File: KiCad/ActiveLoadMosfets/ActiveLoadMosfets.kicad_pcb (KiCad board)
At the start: 2 copper layers, 83.2 x 161.9 mm, 74 parts, among them J1 Conn_01x02_Male, J2 Conn_02x03_Odd_Even, Q1 STP60NF06L, Q2 STP60NF06L, Q3 STP60NF06L, Q4 STP60NF06L, Q5 STP60NF06L, Q6 STP60NF06L, Q7 IRLML2244, Q8 IRLML2244, Q9 IRLML2244, SW1 SW_SPST, SW2 SW_SPDT, U1 LM7322, U2 LM78M12, U3 ATxmega32E5-AU, U4 LED-3digits, U5 LM78M33, U6 SCT2167, U7 SCT2167, U8 LED-3digits

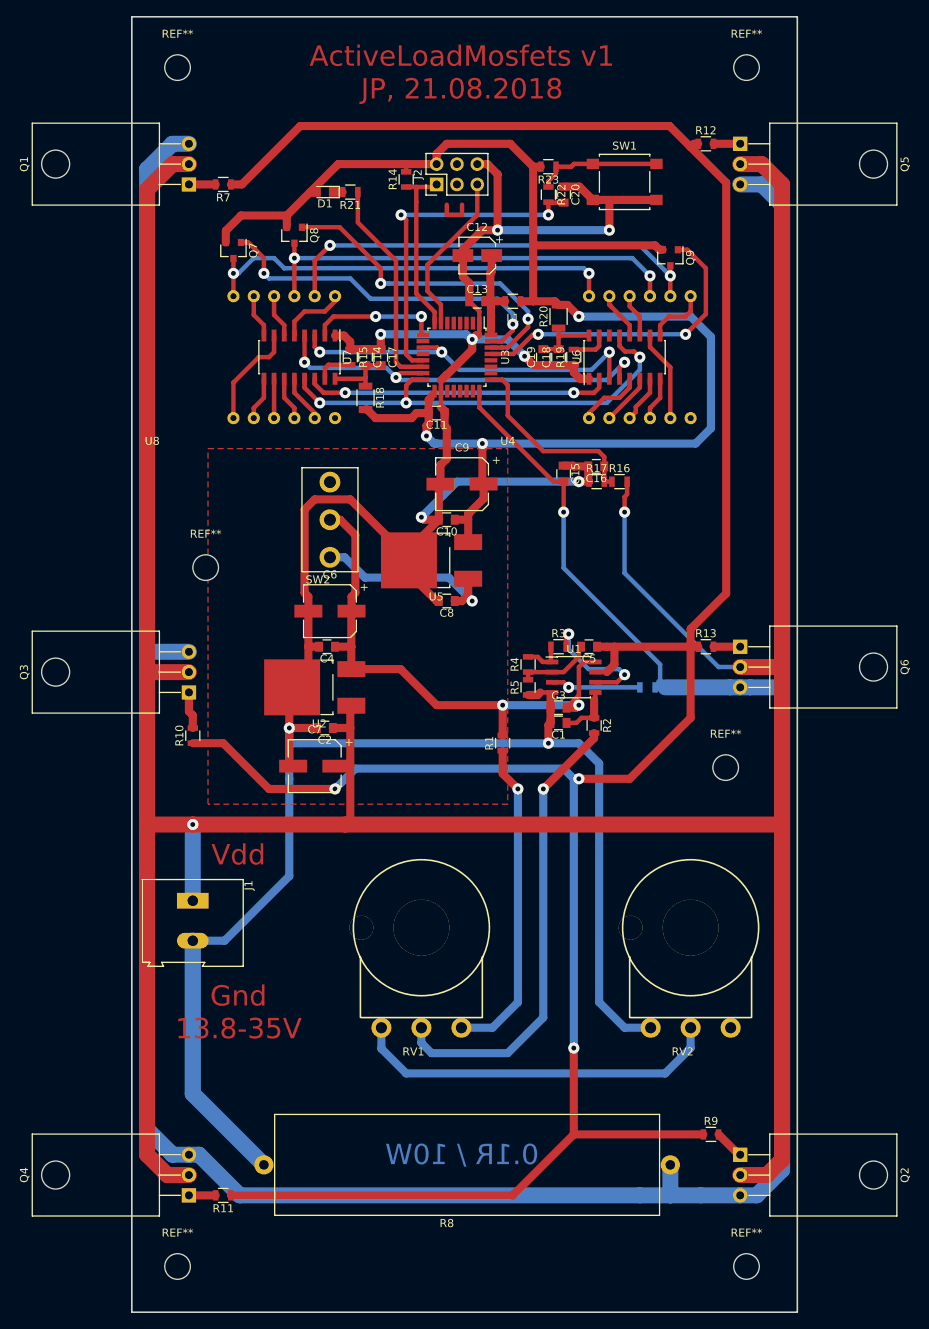
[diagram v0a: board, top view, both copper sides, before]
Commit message: New Atmel Studio project for ActiveLoadMosfets
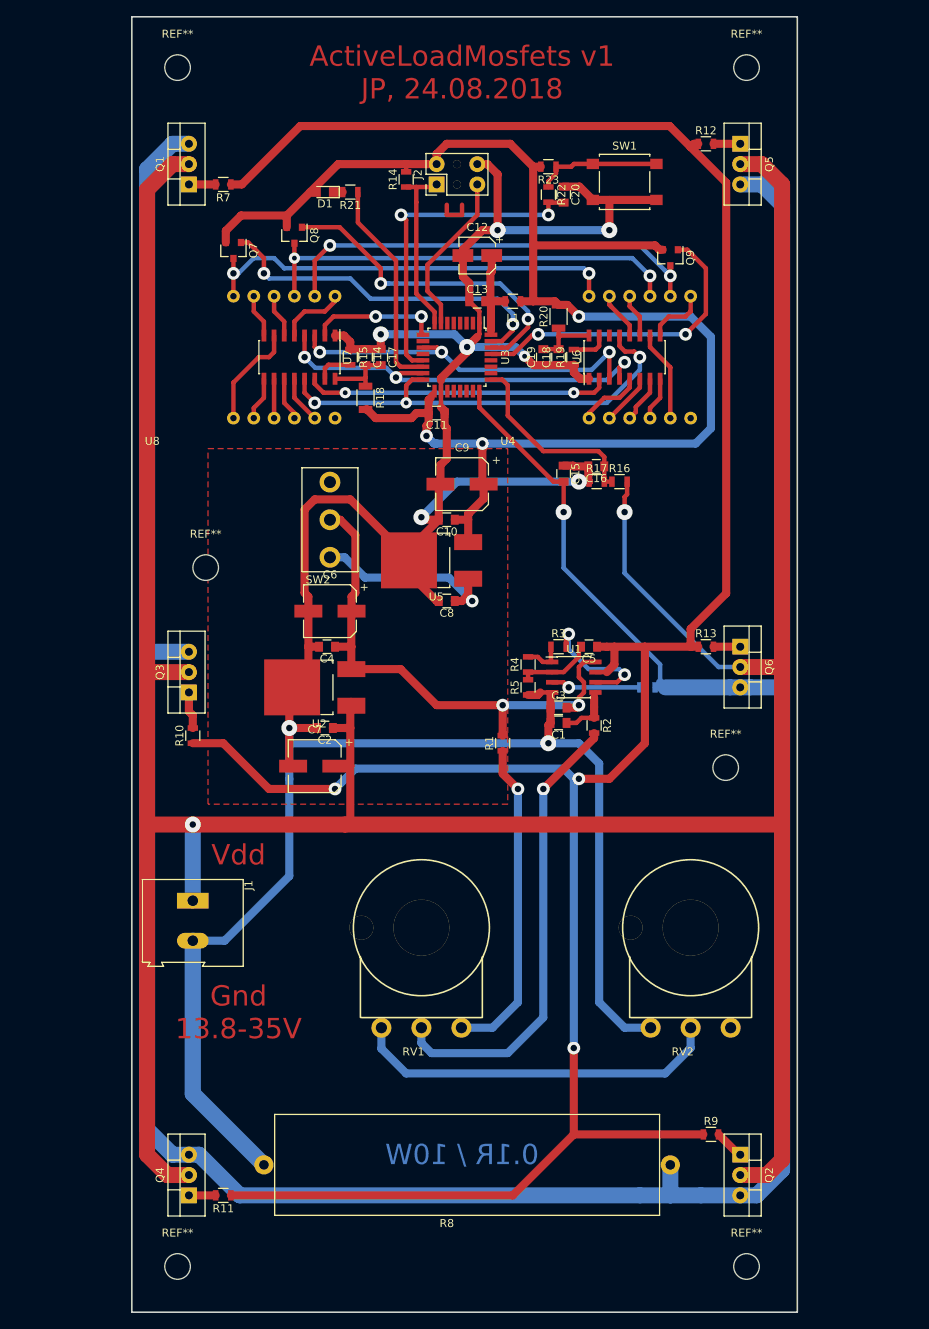
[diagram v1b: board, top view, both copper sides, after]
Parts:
- Q1, Q2, Q3, Q4, Q5, Q6: footprint TO_SOT_Packages_THT:TO-220-3_Horizontal -> TO_SOT_Packages_THT:TO-220-3_Vertical
- U1: value LM7322 -> TLV2372
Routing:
- net Net-(C5-Pad1): track 331.7 -> 327.6 mm
- net GND: track 372.1 -> 371.6 mm
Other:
- net class Default: via_dia 1.4 -> 1.6; via_drill 0.6 -> 0.8
- net class SmallPower: via_dia 1.4 -> 1.6; via_drill 0.6 -> 0.8
- board text added: "ActiveLoadMosfets v1 JP, 24.08.2018"
- board text removed: "ActiveLoadMosfets v1 JP, 21.08.2018"

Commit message: More c++ code, bug fixes on the PCB
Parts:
- added C21: 10u, Capacitors_SMD:CP_Elec_4x5.8, F.Cu at (116.2, 73.0)
- added R24: 1k1, Resistors_SMD:R_0805, F.Cu at (117.5, 68.6)
- C5: value 3n3 -> 1n
- R15, R19: value 1k -> 5k
- R16: value 1k -> 47k
- R17: value 1k -> 1k1
- R4: value 5k -> 5k / 47k ?
- moved L1 6.38 mm to (113.0, 42.5)
- moved C15 2.56 mm to (120.0, 72.7), turned to 90 degrees
- moved R16 2.54 mm to (128.3, 71.4)
- moved R17 2.54 mm to (125.4, 71.4)
- moved C16 2.54 mm to (125.4, 69.5)
- turned SW2 to 180 degrees
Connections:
- C15 pad 2: CURRENT -> Net-(C15-Pad2)
- J2 pad 1: PDI_CLK -> PDI_DATA
- J2 pad 5: PDI_DATA -> PDI_CLK
- Q1 pad 3: CURRENT -> Net-(C15-Pad2)
- Q2 pad 3: CURRENT -> Net-(C15-Pad2)
- Q3 pad 3: CURRENT -> Net-(C15-Pad2)
- Q4 pad 3: CURRENT -> Net-(C15-Pad2)
- Q5 pad 3: CURRENT -> Net-(C15-Pad2)
- Q6 pad 3: CURRENT -> Net-(C15-Pad2)
- R3 pad 2: Net-(R3-Pad2) -> Net-(C5-Pad2)
- R4 pad 1: Net-(C5-Pad2) -> Net-(R4-Pad1)
- R5 pad 2: Net-(C5-Pad2) -> Net-(R4-Pad1)
- R6 pad 1: CURRENT -> Net-(C15-Pad2)
- R8 pad 1: CURRENT -> Net-(C15-Pad2)
- U1 pad 2: Net-(C5-Pad2) -> Net-(R4-Pad1)
- U1 pad 6: Net-(R3-Pad2) -> Net-(C5-Pad2)
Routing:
- net Net-(C15-Pad2): track 0.00 -> 400.1 mm, vias 0 -> 1
- net CURRENT: track 409.9 -> 15.6 mm, vias 1 -> 0
- net Net-(R3-Pad2): track 16.6 -> 0.00 mm, vias 2 -> 0
- net Net-(C5-Pad2): track 9.48 -> 18.5 mm, vias 0 -> 2
- net Net-(C8-Pad1): track 24.9 -> 33.0 mm
- net PDI_CLK: track 21.9 -> 28.9 mm, vias 0 -> 1
- net Net-(R4-Pad1): track 0.00 -> 3.98 mm
- net +3V3: track 187.5 -> 183.8 mm
- net GND: track 371.6 -> 374.6 mm, vias 9 -> 7
- net PDI_DATA: track 20.6 -> 18.0 mm
- net SWITCH: track 42.0 -> 40.9 mm
- net /+3.3Va: track 12.8 -> 13.9 mm
- net VDD: track 416.8 -> 415.7 mm
- net VOLTAGE: track 24.4 -> 25.3 mm
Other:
- board text added: "ActiveLoadMosfets v2-snap JP, 17.09.2018"
- board text removed: "ActiveLoadMosfets v1 JP, 24.08.2018"

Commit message: BCB fixes and cpp code mostly done
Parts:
- Q1: value STP60NF06L -> STP60NF06L / STP9NK60Z
- R15, R19: value 5k -> 15k
- R4: value 5k / 47k ? -> 6k8
- U2: value LM78M12 -> LM78M09
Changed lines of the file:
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@@
       (effects (font (size 1 1) (thickness 0.15)))
     )
-    (fp_text value "5k / 47k ?" (at 0 1.75 90) (layer F.Fab)
+    (fp_text value 6k8 (at 0 1.75 90) (layer F.Fab)
       (effects (font (size 1 1) (thickness 0.15)))
     )
@@
       (effects (font (size 1 1) (thickness 0.15)))
     )
-    (fp_text value LM78M12 (at -0.625 4.8 180) (layer F.Fab)
+    (fp_text value LM78M09 (at -0.625 4.8 180) (layer F.Fab)
       (effects (font (size 1 1) (thickness 0.15)))
     )
@@
       (effects (font (size 1 1) (thickness 0.15)))
     )
-    (fp_text value 5k (at 0 1.75 270) (layer F.Fab)
+    (fp_text value 15k (at 0 1.75 270) (layer F.Fab)
       (effects (font (size 1 1) (thickness 0.15)))
     )
@@
       (effects (font (size 1 1) (thickness 0.15)))
     )
-    (fp_text value 5k (at 0 1.75 90) (layer F.Fab)
+    (fp_text value 15k (at 0 1.75 90) (layer F.Fab)
       (effects (font (size 1 1) (thickness 0.15)))
     )
@@
       (effects (font (size 1 1) (thickness 0.15)))
     )
-    (fp_text value STP60NF06L (at 2.54 3.92 90) (layer F.Fab)
+    (fp_text value "STP60NF06L / STP9NK60Z" (at 2.54 3.92 90) (layer F.Fab)
       (effects (font (size 1 1) (thickness 0.15)))
     )
@@
   (segment (start 120.65 95.885) (end 120.65 94.615) (width 0.5588) (layer F.Cu) (net 4))
   (segment (start 120.65 94.615) (end 121.285 93.98) (width 0.5588) (layer F.Cu) (net 4))
+  (via (at 126.365 95.57) (size 1.6) (drill 0.8) (layers F.Cu B.Cu) (net 5))
+  (segment (start 122.715 96.52) (end 125.415 96.52) (width 0.5588) (layer F.Cu) (net 5))
+  (segment (start 125.415 96.52) (end 126.365 95.57) (width 0.5588) (layer F.Cu) (net 5))
+  (segment (start 119.06 90.175) (end 119.06 92.075) (width 0.5588) (layer F.Cu) (net 5))
+  (via (at 119.38 90.49) (size 1.6) (drill 0.8) (layers F.Cu B.Cu) (net 5))
+  (segment (start 119.38 90.49) (end 119.38 92.395) (width 0.5588) (layer B.Cu) (net 5))
+  (segment (start 119.38 92.395) (end 121.855001 94.870001) (width 0.5588) (layer B.Cu) (net 5))
+  (segment (start 121.855001 94.870001) (end 125.665001 94.870001) (width 0.5588) (layer B.Cu) (net 5))
+  (segment (start 125.665001 94.870001) (end 126.365 95.57) (width 0.5588) (layer B.Cu) (net 5))
+  (segment (start 119.38 90.49) (end 119.06 90.175) (width 0.5588) (layer F.Cu) (net 5))
+  (segment (start 119.06 92.075) (end 120.92 92.075) (width 0.5588) (layer F.Cu) (net 5))
   (segment (start 78.516 34.29) (end 85.816 26.99) (width 1.016) (layer F.Cu) (net 6))
   (segment (start 77.15 34.29) (end 78.516 34.29) (width 1.016) (layer F.Cu) (net 6))
@@
   (segment (start 117.16 93.825) (end 117.315 93.98) (width 0.5588) (layer F.Cu) (net 15))
   (segment (start 117.16 92.075) (end 117.16 93.825) (width 0.5588) (layer F.Cu) (net 15))
-  (via (at 126.365 95.57) (size 1.6) (drill 0.8) (layers F.Cu B.Cu) (net 5))
-  (segment (start 122.715 96.52) (end 125.415 96.52) (width 0.5588) (layer F.Cu) (net 5))
-  (segment (start 125.415 96.52) (end 126.365 95.57) (width 0.5588) (layer F.Cu) (net 5))
-  (segment (start 119.06 90.175) (end 119.06 92.075) (width 0.5588) (layer F.Cu) (net 5))
-  (via (at 119.38 90.49) (size 1.6) (drill 0.8) (layers F.Cu B.Cu) (net 5))
-  (segment (start 119.38 90.49) (end 119.38 92.395) (width 0.5588) (layer B.Cu) (net 5))
-  (segment (start 119.38 92.395) (end 121.855001 94.870001) (width 0.5588) (layer B.Cu) (net 5))
-  (segment (start 121.855001 94.870001) (end 125.665001 94.870001) (width 0.5588) (layer B.Cu) (net 5))
-  (segment (start 125.665001 94.870001) (end 126.365 95.57) (width 0.5588) (layer B.Cu) (net 5))
-  (segment (start 119.38 90.49) (end 119.06 90.175) (width 0.5588) (layer F.Cu) (net 5))
-  (segment (start 119.06 92.075) (end 120.92 92.075) (width 0.5588) (layer F.Cu) (net 5))
   (via (at 119.38 97.155) (size 1.6) (drill 0.8) (layers F.Cu B.Cu) (net 16))
   (segment (start 117.315 96.52) (end 118.745 96.52) (width 0.5588) (layer F.Cu) (net 16))
@@
   (segment (start 116.205 66.675) (end 116.205 68.58) (width 0.5588) (layer F.Cu) (net 19))
   (segment (start 116.205 68.58) (end 116.205 71.225) (width 0.5588) (layer F.Cu) (net 19))
-  (segment (start 71.905 92.71) (end 66.675 92.71) (width 2) (layer B.Cu) (net 60))
-  (segment (start 146.05 157.48) (end 142.875 160.655) (width 2) (layer B.Cu) (net 60))
-  (segment (start 142.875 160.655) (end 140.82 160.655) (width 2) (layer B.Cu) (net 60))
-  (segment (start 142.092792 97.155) (end 146.05 97.155) (width 2) (layer B.Cu) (net 60))
-  (segment (start 140.82 97.155) (end 142.092792 97.155) (width 2) (layer B.Cu) (net 60))
-  (segment (start 146.05 97.155) (end 146.05 157.48) (width 2) (layer B.Cu) (net 60))
-  (segment (start 140.82 160.655) (end 135.89 160.655) (width 2) (layer B.Cu) (net 60))
-  (segment (start 66.675 32.385) (end 66.675 92.71) (width 2) (layer B.Cu) (net 60))
-  (segment (start 71.905 29.21) (end 69.85 29.21) (width 2) (layer B.Cu) (net 60))
-  (segment (start 69.85 29.21) (end 66.675 32.385) (width 2) (layer B.Cu) (net 60))
-  (segment (start 69.85 155.575) (end 71.905 155.575) (width 2) (layer B.Cu) (net 60))
-  (segment (start 66.675 92.71) (end 66.675 152.4) (width 2) (layer B.Cu) (net 60))
-  (segment (start 66.675 152.4) (end 69.85 155.575) (width 2) (layer B.Cu) (net 60))
-  (segment (start 140.82 34.29) (end 143.51 34.29) (width 2) (layer B.Cu) (net 60))
-  (segment (start 143.51 34.29) (end 146.05 36.83) (width 2) (layer B.Cu) (net 60))
-  (segment (start 146.05 36.83) (end 146.05 97.155) (width 2) (layer B.Cu) (net 60))
-  (segment (start 140.82 97.155) (end 139.547208 97.155) (width 2) (layer B.Cu) (net 60))
-  (segment (start 139.547208 97.155) (end 131.445 97.155) (width 2) (layer B.Cu) (net 60))
-  (segment (start 131.445 97.155) (end 130.81 96.52) (width 1.016) (layer B.Cu) (net 60))
-  (segment (start 130.175 97.155) (end 131.445 97.155) (width 0.5588) (layer B.Cu) (net 60))
-  (segment (start 78.257792 160.655) (end 128.27 160.655) (width 2) (layer B.Cu) (net 60))
-  (segment (start 71.905 155.575) (end 73.177792 155.575) (width 2) (layer B.Cu) (net 60))
-  (segment (start 73.177792 155.575) (end 78.257792 160.655) (width 2) (layer B.Cu) (net 60))
-  (segment (start 132.08 156.845) (end 132.08 160.655) (width 2) (layer B.Cu) (net 60))
-  (segment (start 128.27 160.655) (end 132.08 160.655) (width 2) (layer B.Cu) (net 60))
-  (segment (start 132.08 160.655) (end 135.89 160.655) (width 2) (layer B.Cu) (net 60))
   (segment (start 127.32 71.44) (end 126.365 71.44) (width 0.5588) (layer F.Cu) (net 20))
   (segment (start 126.365 71.44) (end 126.365 69.535) (width 0.5588) (layer F.Cu) (net 20))
@@
   (segment (start 92.455 71.5) (end 107.315 86.36) (width 1.016) (layer B.Cu) (net 59))
   (segment (start 89.535 71.5) (end 92.455 71.5) (width 1.016) (layer B.Cu) (net 59))
+  (segment (start 71.905 92.71) (end 66.675 92.71) (width 2) (layer B.Cu) (net 60))
+  (segment (start 146.05 157.48) (end 142.875 160.655) (width 2) (layer B.Cu) (net 60))
+  (segment (start 142.875 160.655) (end 140.82 160.655) (width 2) (layer B.Cu) (net 60))
+  (segment (start 142.092792 97.155) (end 146.05 97.155) (width 2) (layer B.Cu) (net 60))
+  (segment (start 140.82 97.155) (end 142.092792 97.155) (width 2) (layer B.Cu) (net 60))
+  (segment (start 146.05 97.155) (end 146.05 157.48) (width 2) (layer B.Cu) (net 60))
+  (segment (start 140.82 160.655) (end 135.89 160.655) (width 2) (layer B.Cu) (net 60))
+  (segment (start 66.675 32.385) (end 66.675 92.71) (width 2) (layer B.Cu) (net 60))
+  (segment (start 71.905 29.21) (end 69.85 29.21) (width 2) (layer B.Cu) (net 60))
+  (segment (start 69.85 29.21) (end 66.675 32.385) (width 2) (layer B.Cu) (net 60))
+  (segment (start 69.85 155.575) (end 71.905 155.575) (width 2) (layer B.Cu) (net 60))
+  (segment (start 66.675 92.71) (end 66.675 152.4) (width 2) (layer B.Cu) (net 60))
+  (segment (start 66.675 152.4) (end 69.85 155.575) (width 2) (layer B.Cu) (net 60))
+  (segment (start 140.82 34.29) (end 143.51 34.29) (width 2) (layer B.Cu) (net 60))
+  (segment (start 143.51 34.29) (end 146.05 36.83) (width 2) (layer B.Cu) (net 60))
+  (segment (start 146.05 36.83) (end 146.05 97.155) (width 2) (layer B.Cu) (net 60))
+  (segment (start 140.82 97.155) (end 139.547208 97.155) (width 2) (layer B.Cu) (net 60))
+  (segment (start 139.547208 97.155) (end 131.445 97.155) (width 2) (layer B.Cu) (net 60))
+  (segment (start 131.445 97.155) (end 130.81 96.52) (width 1.016) (layer B.Cu) (net 60))
+  (segment (start 130.175 97.155) (end 131.445 97.155) (width 0.5588) (layer B.Cu) (net 60))
+  (segment (start 78.257792 160.655) (end 128.27 160.655) (width 2) (layer B.Cu) (net 60))
+  (segment (start 71.905 155.575) (end 73.177792 155.575) (width 2) (layer B.Cu) (net 60))
+  (segment (start 73.177792 155.575) (end 78.257792 160.655) (width 2) (layer B.Cu) (net 60))
+  (segment (start 132.08 156.845) (end 132.08 160.655) (width 2) (layer B.Cu) (net 60))
+  (segment (start 128.27 160.655) (end 132.08 160.655) (width 2) (layer B.Cu) (net 60))
+  (segment (start 132.08 160.655) (end 135.89 160.655) (width 2) (layer B.Cu) (net 60))
   (via (at 120.65 69.215) (size 2) (drill 0.8) (layers F.Cu B.Cu) (net 60))
   (segment (start 130.81 94.3) (end 130.81 96.52) (width 0.5588) (layer B.Cu) (net 60))
